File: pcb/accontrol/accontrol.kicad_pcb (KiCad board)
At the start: 2 copper layers, 56 x 40 mm, 34 parts, among them J1 CTRL, J2 MAINS_IN, J3 VALVE, J4 PUMP, Q1 SS8050, Q2 BT136S-600E, Q3 SS8050, Q4 BT136S-600E, U1 MOC3043M, U2 MOC3023M, U3 EL817C

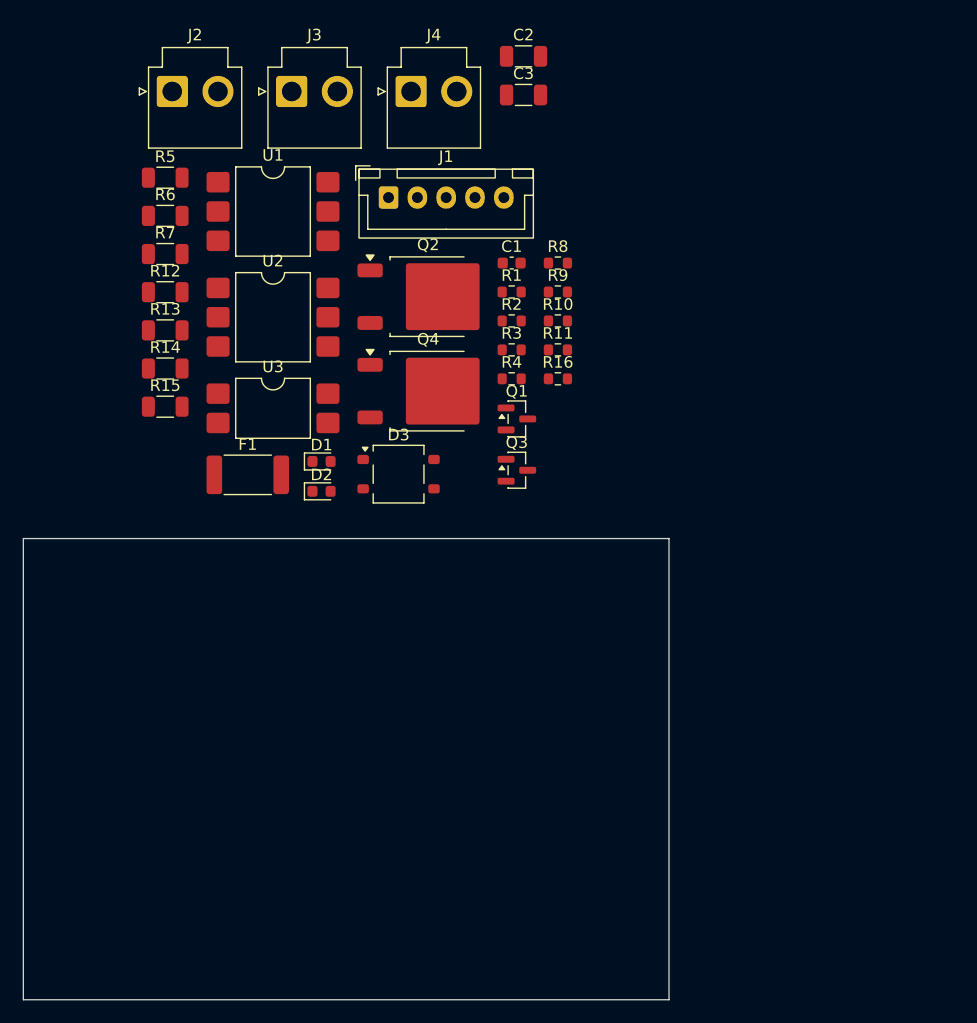
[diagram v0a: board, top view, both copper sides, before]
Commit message: Shelve the AC control board with its layout study
The machine keeps the RobotDyn dimmer and the M5Stack Unit SSR. A single
board with both channels, the zero-cross sense and the fuse needs about
80 x 30 mm, while the AC enclosure offers 68 x 31.6 mm inside, and the
single cable it would bring did not justify a home-made 230 V board.

Keep the work as a reference: AC and Mains net classes with DRC rules for
2.5 mm between mains nets and 7 mm to the 3V3 side, slotted optocoupler
footprints, HT396R right-angle headers, an AEM 2410 fuse (100 A breaking),
1210 resistors for the zero-cross divider and the pump snubber, L_IN
between J2 and F1, and the partial valve-channel layout.

Co-Authored-By: Claude Opus 5.5 <noreply@anthropic.com>
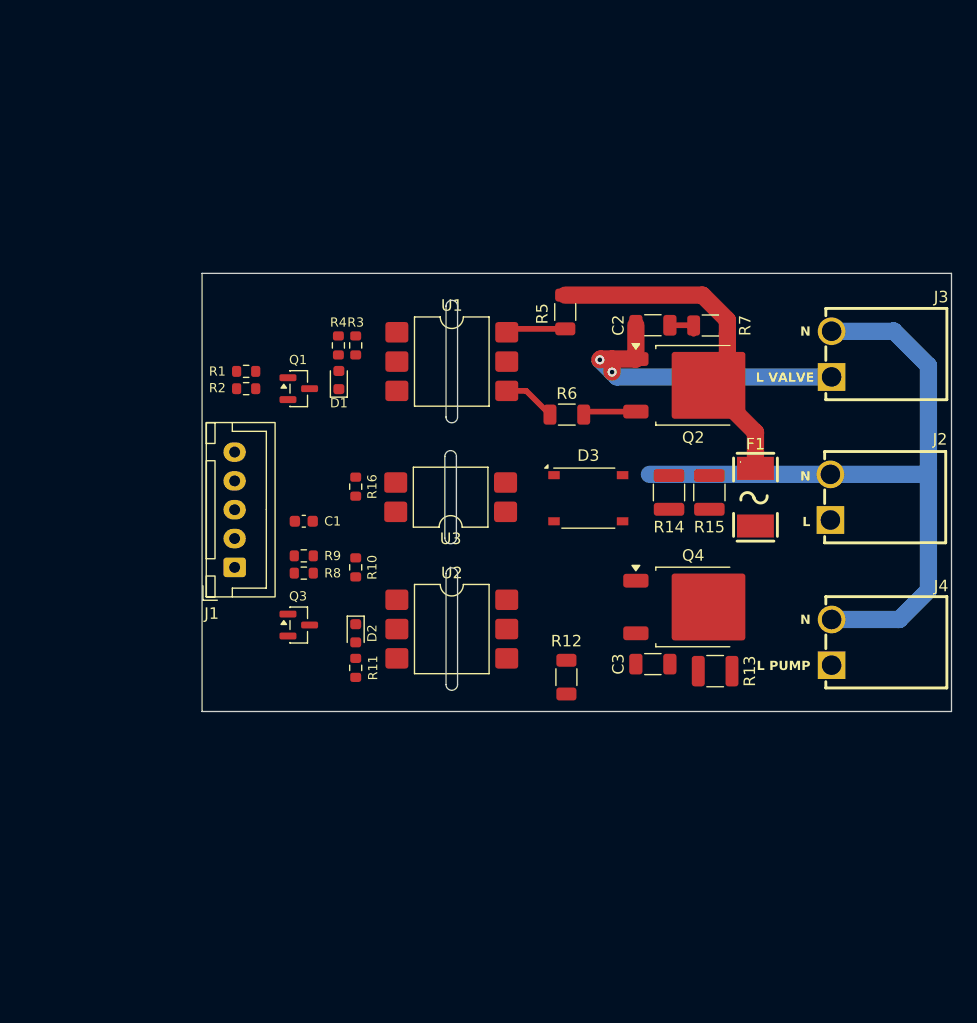
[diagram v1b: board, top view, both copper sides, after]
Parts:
- D3: footprint Package_TO_SOT_SMD:TO-269AA -> Diode_SMD:Diode_Bridge_Diotec_ABS
- F1: footprint Fuse:Fuse_2512_6332Metric -> Accontrol_Local:F2410
- J2, J3, J4: footprint Connector_JST:JST_VH_B2P-VH_1x02_P3.96mm_Vertical -> Accontrol_Local:CONN-TH_P3.96_HT396R-3.96-2P
- Q2, Q4: value BT136S-600E -> BT136S
- R13, R14, R15: footprint Resistor_SMD:R_1206_3216Metric -> Resistor_SMD:R_1210_3225Metric
- U1, U2: footprint Package_DIP:SMDIP-6_W9.53mm -> Accontrol_Local:SMDIP-6_W9.53mm_Slot
- U3: footprint Package_DIP:SMDIP-4_W9.53mm -> Accontrol_Local:SMDIP-4_W9.53mm_Slot
- moved J2 67.1 mm to (135.0, 66.4), turned to 90 degrees
- moved J4 60.1 mm to (135.1, 79.0), turned to 90 degrees
- moved R13 56.1 mm to (125.0, 81.5), turned to 180 degrees
- moved J3 52.1 mm to (135.1, 54.0), turned to 90 degrees
- moved C3 50.6 mm to (119.6, 80.9), turned to 180 degrees
- moved R12 48.2 mm to (112.1, 82.0), turned to -90 degrees
- moved R15 47.8 mm to (124.5, 66.0), turned to 90 degrees
- moved R7 47.7 mm to (124.6, 51.5), turned to 180 degrees
- moved R14 45.0 mm to (121.0, 66.0), turned to -90 degrees
- moved F1 44.1 mm to (128.5, 66.4), turned to -90 degrees
- moved R6 38.9 mm to (112.1, 59.2)
- moved R5 36.6 mm to (112.0, 50.4), turned to 90 degrees
- moved R8 34.8 mm to (89.3, 73.0)
- moved J1 34.7 mm to (83.3, 72.5), turned to 90 degrees
- moved R11 32.7 mm to (93.8, 81.2), turned to 90 degrees
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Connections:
- net Net-(J2-Pin_1) renamed /L_IN
- J1 pad 3: /ZC -> /DIM
- J1 pad 4: /DIM -> /ZC
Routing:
- net /N: track 0.00 -> 63.0 mm
- net /L: track 0.00 -> 30.2 mm
- net /L_VALVE: track 0.00 -> 27.9 mm, vias 0 -> 2
- net Net-(R5-Pad1): track 0.00 -> 5.38 mm
- net Net-(Q2-G): track 0.00 -> 4.63 mm
- net Net-(R6-Pad1): track 0.00 -> 4.60 mm
- net Net-(C2-Pad1): track 0.00 -> 2.10 mm
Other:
- board size 56 x 40 mm -> 65 x 38 mm
- board text added: "L"
- board text added: "L PUMP"
- board text added: "L VALVE"
- board text added: "N"
